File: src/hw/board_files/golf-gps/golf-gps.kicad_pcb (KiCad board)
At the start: 4 copper layers, 71.6 x 92.1 mm, 63 parts, among them J1 USB_C_Receptacle_PowerOnly_6P, J3 Micro_SD_Card, SW1 SW_SPDT, SW2 RESET, SW3 BOOT, SW4 BTN_1, SW5 BTN_2, SW6 BTN_3, U1 MCP73831-2-OT, U2 TPS63031DSKR, U3 STM32L432KCU6, U4 NEO-M9N, Y1 32.768kHz

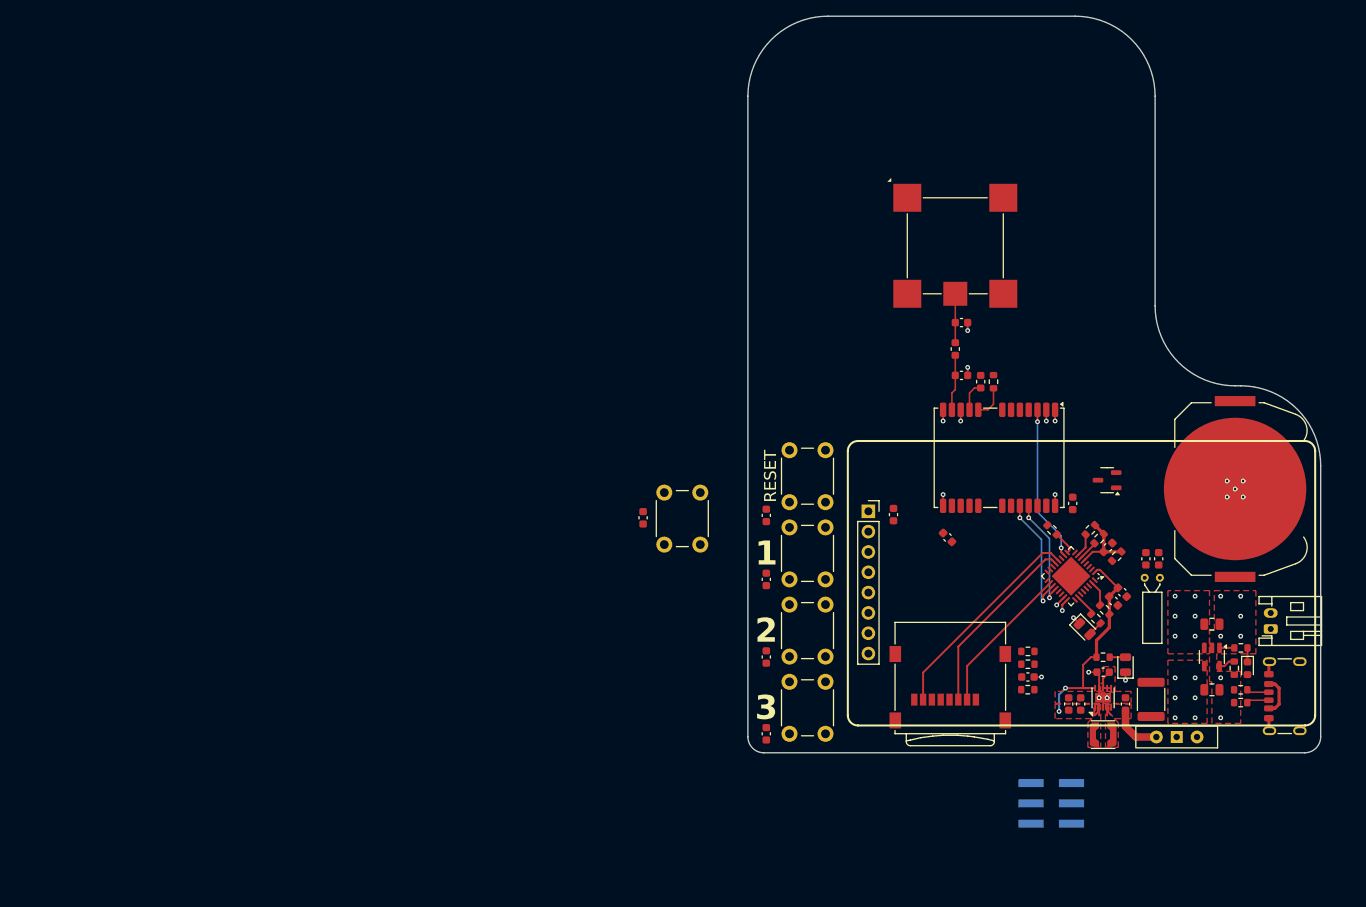
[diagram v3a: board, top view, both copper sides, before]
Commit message: Finished new sch. Updated pinout. Started new PCB.
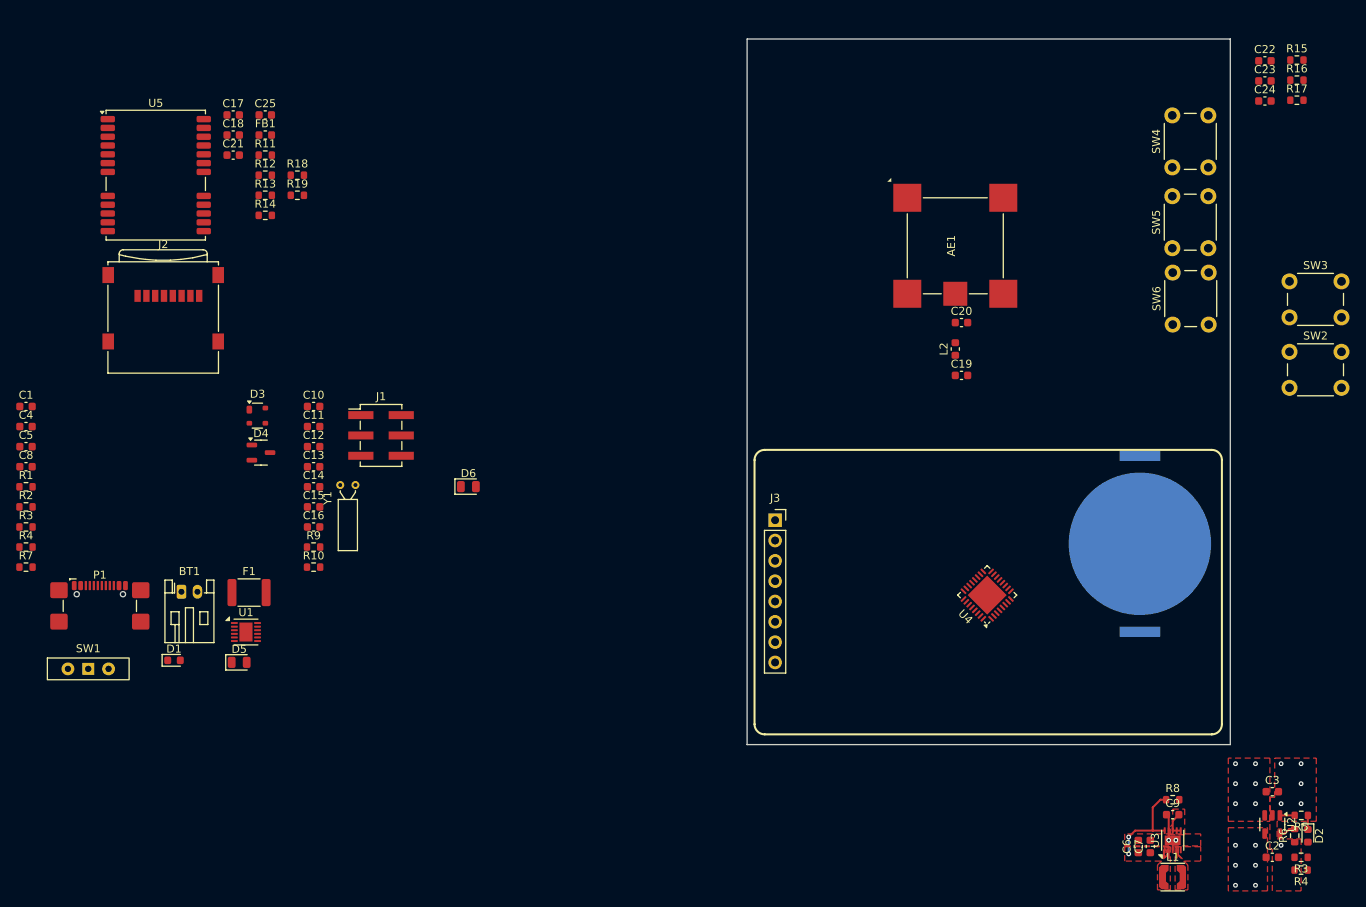
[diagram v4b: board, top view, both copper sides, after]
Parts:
- removed the C19 at (112.3, 134.0)
- removed the C20 at (112.3, 143.7)
- removed the C7 at (156.8, 135.6)
- removed the C9 at (155.0, 130.0)
- removed the J3 at (135.3, 147.5)
- removed the R6 at (156.1, 131.1)
- removed the R8 at (145.0, 147.8)
- removed the U3 at (150.4, 133.6)
- added C1: 100n, Capacitor_SMD:C_0603_1608Metric, F.Cu at (19.8, 112.4)
- added C16: TBD, Capacitor_SMD:C_0603_1608Metric, F.Cu at (55.7, 127.4)
- added C17: 100n, Capacitor_SMD:C_0603_1608Metric, F.Cu at (45.7, 75.9)
- added C23: 100n, Capacitor_SMD:C_0603_1608Metric, F.Cu at (174.6, 71.7)
- added C24: 100n, Capacitor_SMD:C_0603_1608Metric, F.Cu at (174.6, 74.2)
- added C25: 100n, Capacitor_SMD:C_0603_1608Metric, F.Cu at (49.7, 75.9)
- added C4: 47p, Capacitor_SMD:C_0603_1608Metric, F.Cu at (19.8, 114.9)
- added D5: LED_PWR, LED_SMD:LED_0805_2012Metric, F.Cu at (46.4, 144.4)
- added D6: LED_STATUS, LED_SMD:LED_0805_2012Metric, F.Cu at (75.1, 122.4)
- added P1: USB_C_Plug_USB2.0, Connector_USB:USB_C_Receptacle_GCT_USB4110, F.Cu at (29.0, 138.5)
- added R1: 27R, Resistor_SMD:R_0603_1608Metric, F.Cu at (19.8, 122.4)
- added R16: 10k, Resistor_SMD:R_0603_1608Metric, F.Cu at (178.6, 71.6)
- added R17: 10k, Resistor_SMD:R_0603_1608Metric, F.Cu at (178.6, 74.1)
- added R18: 10k, Resistor_SMD:R_0603_1608Metric, F.Cu at (53.7, 83.5)
- added R19: 10k, Resistor_SMD:R_0603_1608Metric, F.Cu at (53.7, 86.0)
- added R2: 27R, Resistor_SMD:R_0603_1608Metric, F.Cu at (19.8, 124.9)
- added R3: 1k, Resistor_SMD:R_0603_1608Metric, F.Cu at (19.8, 127.4)
- added R4: 10k, Resistor_SMD:R_0603_1608Metric, F.Cu at (19.8, 130.0)
- added U1: FT234XD-R, Package_DFN_QFN:DFN-12-1EP_3x3mm_P0.45mm_EP1.65x2.38mm, F.Cu at (47.3, 140.6)
- added U5: NEO-M9N, RF_GPS:ublox_NEO, F.Cu at (36.0, 83.5)
- BT1: value CR2032 -> LiPo; footprint Battery:BatteryHolder_Keystone_3034_1x20mm -> Connector_JST:JST_PH_S2B-PH-K_1x02_P2.00mm_Horizontal
- BT2: value LiPo -> CR2032; footprint Connector_JST:JST_PH_S2B-PH-K_1x02_P2.00mm_Horizontal -> Battery:BatteryHolder_Keystone_3034_1x20mm; moved to B.Cu
- C10: value 100n -> 2u2
- C12, C13: value TBD -> 100n
- C15: value 100n -> TBD
- C2: renamed from C1; footprint Capacitor_SMD:C_0805_2012Metric -> Capacitor_SMD:C_0603_1608Metric
- C3: renamed from C2; footprint Capacitor_SMD:C_0805_2012Metric -> Capacitor_SMD:C_0603_1608Metric
- C5: value 10u -> 47p
- C8: value 100n -> 10u
- D1: value BAT54C -> TX_LED; footprint Package_TO_SOT_SMD:SOT-23-3 -> LED_SMD:LED_0603_1608Metric
- D3: value LED_PWR -> PRTR5V0U2X; footprint LED_SMD:LED_0805_2012Metric -> Package_TO_SOT_SMD:SOT-143
- D4: value LED_STATUS -> BAT54C; footprint LED_SMD:LED_0805_2012Metric -> Package_TO_SOT_SMD:SOT-23-3
- J1: value USB_C_Receptacle_PowerOnly_6P -> ~; footprint Connector_USB:USB_C_Receptacle_GCT_USB4125-xx-x-0190_6P_TopMnt_Horizontal -> Connector_PinHeader_2.54mm:PinHeader_2x03_P2.54mm_Vertical_SMD
- J2: value ~ -> Micro_SD_Card; footprint Connector_PinHeader_2.54mm:PinHeader_2x03_P2.54mm_Vertical_SMD -> Connector_Card:microSD_HC_Wuerth_693072010801; moved to F.Cu
- R10: value 10k -> 330R
- R7: value 330R -> 5k1
- U4: value NEO-M9N -> STM32L432KCU6; footprint RF_GPS:ublox_NEO -> Package_DFN_QFN:QFN-32-1EP_5x5mm_P0.5mm_EP3.45x3.45mm
- moved C5 141.2 mm to (19.8, 117.4), turned to 0 degrees
- moved C8 137.0 mm to (19.8, 119.9), turned to 0 degrees
- moved SW1 136.3 mm to (27.5, 145.2), turned to 0 degrees
- moved R7 133.9 mm to (19.8, 132.5), turned to 0 degrees
- moved BT1 132.3 mm to (39.2, 135.5), turned to 0 degrees
- moved J2 127.1 mm to (36.9, 100.1), turned to 0 degrees
- moved D1 118.8 mm to (38.3, 144.1), turned to 0 degrees
- moved J1 118.6 mm to (64.1, 116.0), turned to 0 degrees
- moved R12 118.2 mm to (49.7, 83.5), turned to 0 degrees
- moved F1 113.5 mm to (47.6, 135.6), turned to 0 degrees
- moved D3 112.9 mm to (48.7, 113.5), turned to 0 degrees
- moved R13 112.7 mm to (49.7, 86.0), turned to 0 degrees
- moved R14 110.4 mm to (49.7, 88.5), turned to 0 degrees
- moved C12 106.6 mm to (55.7, 117.4), turned to 0 degrees
- moved D4 105.3 mm to (49.1, 118.2), turned to 0 degrees
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- renumbered C16 to C19, C17 to C20, C3 to C6, C4 to C7, C6 to C9, J4 to J3, R1 to R5, R2 to R6, R5 to R8, U1 to U2, U2 to U3
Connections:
- BT1 pad 1: Net-(BT1-+) -> VBAT
- BT2 pad 1: VBAT -> Net-(BT2-+)
- C11 pad 1: GND -> +3V3
- C11 pad 2: /Microcontroller/NRST -> GND
- C12 pad 1: Net-(U3-PC14) -> +3V3
- C13 pad 1: Net-(U3-PC15) -> +3V3
- C14 pad 1: +3V3 -> GND
- C14 pad 2: GND -> /Microcontroller/NRST
- C15 pad 1: +3V3 -> /Microcontroller/OSC32_IN
- C18 pad 1: GND -> +3V3
- C18 pad 2: /Microcontroller/BOOT -> GND
- C19 pad 1: Net-(U4-RF_IN) -> Net-(U5-RF_IN)
- C2 pad 1: /Power/V_USB -> V_USB
- C21 pad 1: GND -> /Microcontroller/BOOT0
- C21 pad 2: /Microcontroller/BTN_3 -> +3V3
- C22 pad 1: +3V3 -> GND
- C22 pad 2: GND -> /Microcontroller/BTN_1
- C5 pad 1: Net-(SW1-A) -> /Power/USB_D-
- C8 pad 1: +3V3 -> Net-(SW1-A)
- D1 pad 1: +3V3 -> Net-(D1-K)
- D1 pad 2: Net-(BT1-+) -> Net-(D1-A)
- D2 pad 2: /Power/V_USB -> V_USB
- D3 pad 2: Net-(D3-A) -> /Power/USB_D+
- D4 pad 1: GND -> +3V3
- D4 pad 2: Net-(D4-A) -> Net-(BT2-+)
- FB1 pad 1: Net-(U4-VCC_RF) -> Net-(U5-VCC_RF)
- J2 pad 1: +3V3 -> unconnected-(J2-DAT2-Pad1)
- J2 pad 2: /Microcontroller/SWDIO -> /Microcontroller/SD_CS
- J2 pad 3: GND -> /Microcontroller/SPI3_MOSI
- J2 pad 4: /Microcontroller/SWCLK -> +3V3
- J2 pad 5: GND -> /Microcontroller/SPI3_SCK
- J2 pad 6: /Microcontroller/NRST -> GND
- J3 pad 1: +3V3 -> Net-(J3-BL)
- J3 pad 4: +3V3 -> Net-(J3-BL)
- J3 pad 5: /Microcontroller/SPI_MOSI -> /Microcontroller/SPI3_MOSI
- J3 pad 6: /Microcontroller/SPI_SCK -> /Microcontroller/SPI3_SCK
- L2 pad 1: Net-(U4-RF_IN) -> Net-(U5-RF_IN)
- R10 pad 1: +3V3 -> /Microcontroller/LED_STATUS
- R10 pad 2: /Microcontroller/SPI_MISO -> Net-(D6-A)
- R11 pad 1: Net-(U4-~{RESET}) -> +3V3
- R11 pad 2: +3V3 -> /Microcontroller/SD_CS
- R12 pad 2: /Microcontroller/BOOT -> /Microcontroller/SPI3_MOSI
- R13 pad 1: /Microcontroller/BTN_1 -> +3V3
- R13 pad 2: +3V3 -> /Microcontroller/SPI3_MISO
- R14 pad 1: /Microcontroller/BTN_2 -> Net-(U5-~{RESET})
- R15 pad 1: /Microcontroller/BTN_3 -> /Microcontroller/BTN_1
- R7 pad 1: Net-(U3-PB3) -> GND
- R7 pad 2: Net-(D4-A) -> Net-(P1-CC)
- R8 pad 2: Net-(D3-A) -> Net-(D5-A)
- R9 pad 2: /Microcontroller/SPI_MOSI -> /Microcontroller/NRST
- SW3 pad 1: /Microcontroller/BOOT -> +3V3
- SW3 pad 2: GND -> /Microcontroller/BOOT0
- U2 pad 4: /Power/V_USB -> V_USB
- U4 pad 1: GND -> +3V3
- U4 pad 10: GND -> /Microcontroller/GPS_PPS
- U4 pad 11: Net-(U4-RF_IN) -> unconnected-(U4-PA5-Pad11)
- U4 pad 12: GND -> /Microcontroller/BTN_3
- U4 pad 13: GND -> /Microcontroller/BTN_2
- U4 pad 14: unconnected-(U4-LNA_EN-Pad14) -> /Microcontroller/BTN_1
- U4 pad 15: unconnected-(U4-RESERVED-Pad15) -> /Microcontroller/LED_STATUS
- U4 pad 16: unconnected-(U4-RESERVED-Pad16) -> GND
- U4 pad 17: unconnected-(U4-RESERVED-Pad17) -> +3V3
- U4 pad 19: unconnected-(U4-SCL/SPI_CLK-Pad19) -> /Microcontroller/GPS_RX
- U4 pad 2: GND -> /Microcontroller/OSC32_IN
- U4 pad 20: /Microcontroller/GPS_RX -> /Microcontroller/GPS_TX
- U4 pad 21: /Microcontroller/GPS_TX -> /Microcontroller/LCD_CS
- U4 pad 22: V_BCKP -> /Microcontroller/LCD_DC
- U4 pad 23: +3V3 -> /Microcontroller/SWDIO
- U4 pad 24: GND -> /Microcontroller/SWCLK
- U4 pad 3: /Microcontroller/GPS_PPS -> /Microcontroller/OSC32_OUT
- U4 pad 4: unconnected-(U4-EXTINT-Pad4) -> /Microcontroller/NRST
- U4 pad 5: unconnected-(U4-USB_DM-Pad5) -> +3V3
- U4 pad 8: Net-(U4-~{RESET}) -> /Microcontroller/USART2_TX
- U4 pad 9: Net-(U4-VCC_RF) -> /Microcontroller/USART2_RX
- Y1 pad 1: Net-(U3-PC15) -> /Microcontroller/OSC32_OUT
- Y1 pad 2: Net-(U3-PC14) -> /Microcontroller/OSC32_IN
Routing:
- net /Microcontroller/SPI_MISO: track 26.9 -> 0.00 mm
- net /Microcontroller/SPI_MOSI: track 23.6 -> 0.00 mm
- net +3V3: track 36.5 -> 13.0 mm
- net /Microcontroller/GPS_PPS: track 19.6 -> 0.00 mm, vias 2 -> 0
- net /Microcontroller/SD_CS: track 18.9 -> 0.00 mm
- net GND: track 22.6 -> 4.73 mm, vias 26 -> 8
- net /Microcontroller/GPS_RX: track 15.5 -> 0.00 mm, vias 2 -> 0
- net /Microcontroller/GPS_TX: track 14.1 -> 0.00 mm, vias 2 -> 0
- net Net-(U4-RF_IN): track 6.99 -> 0.00 mm
- net Net-(SW1-A): track 6.30 -> 0.00 mm
- net Net-(AE1-A): track 6.11 -> 0.00 mm
- net /Power/V_USB: track 4.99 -> 0.00 mm, vias 6 -> 0
- net Net-(U4-~{RESET}): track 4.18 -> 0.00 mm
- net Net-(U4-VCC_RF): track 3.76 -> 0.00 mm
- net /Microcontroller/BOOT: track 3.19 -> 0.00 mm
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- added copper zone on In2.Cu, net +3V3
- added copper zone on F.Cu, net V_USB
- removed copper zone on F.Cu, net /Power/V_USB
- removed copper zone on In2.Cu, net GND
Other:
- board size 71.6 x 92.1 mm -> 60.4 x 88.2 mm
- board text removed: "1"
- board text removed: "2"
- board text removed: "3"
- board text removed: "RESET"

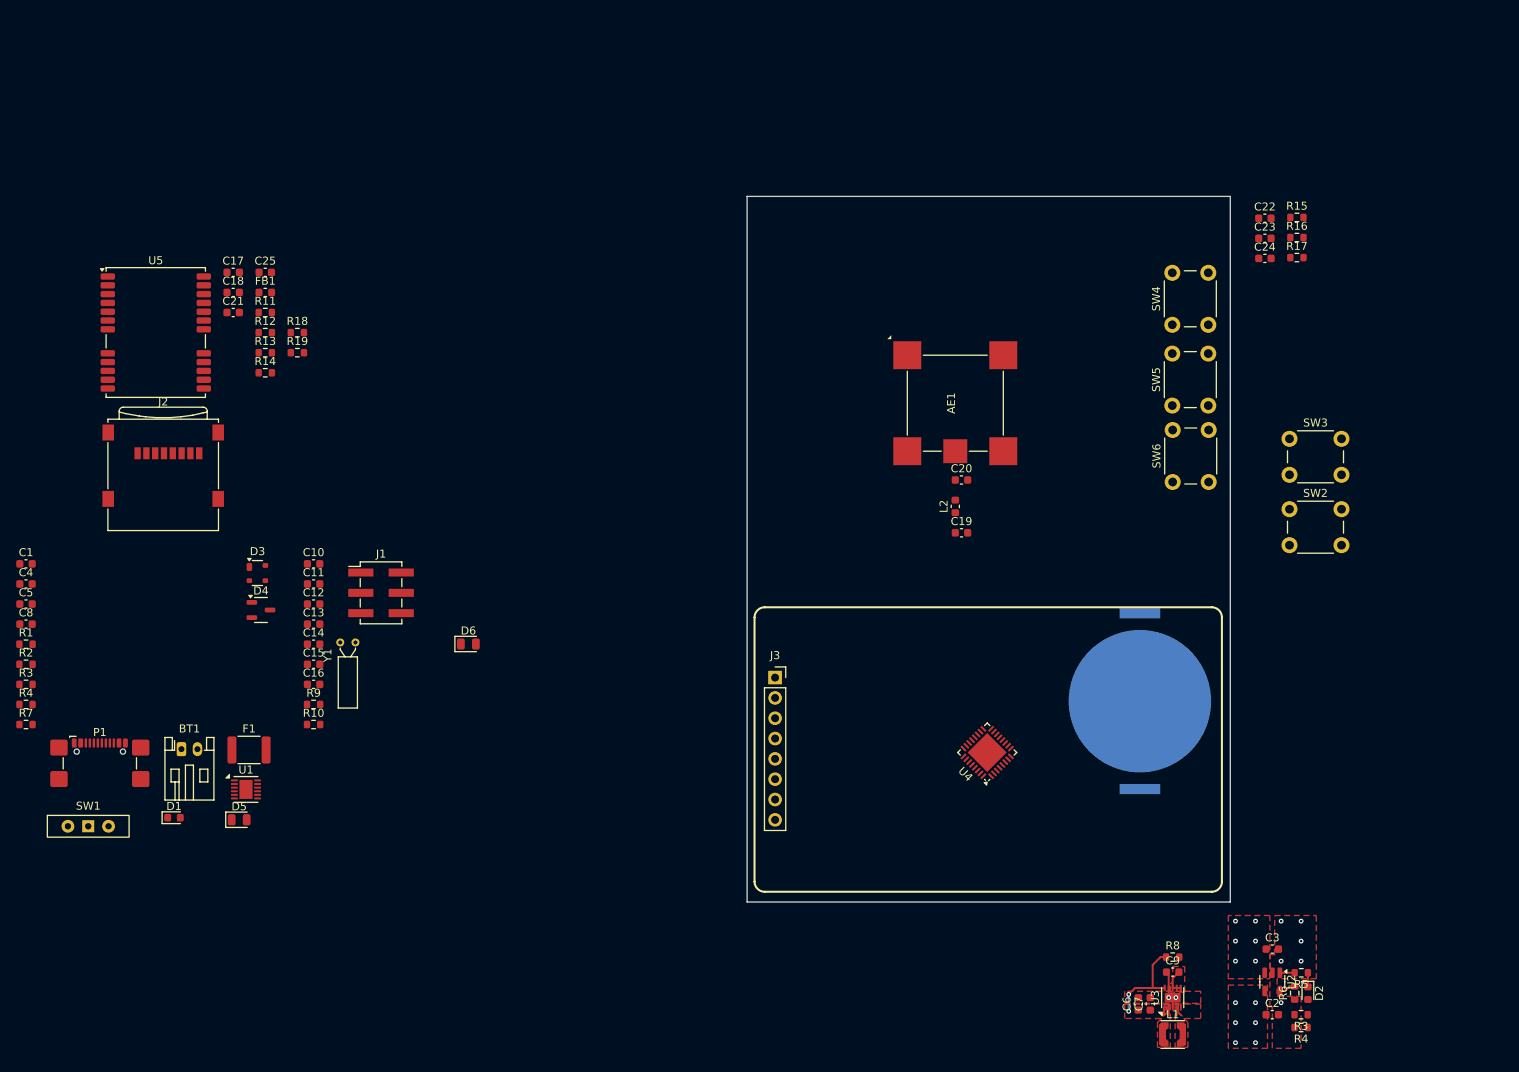
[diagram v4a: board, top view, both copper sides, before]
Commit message: Removed USB to UART bridge, added VDDA decoupling, adjusted MCU pinout and updated spreadsheet
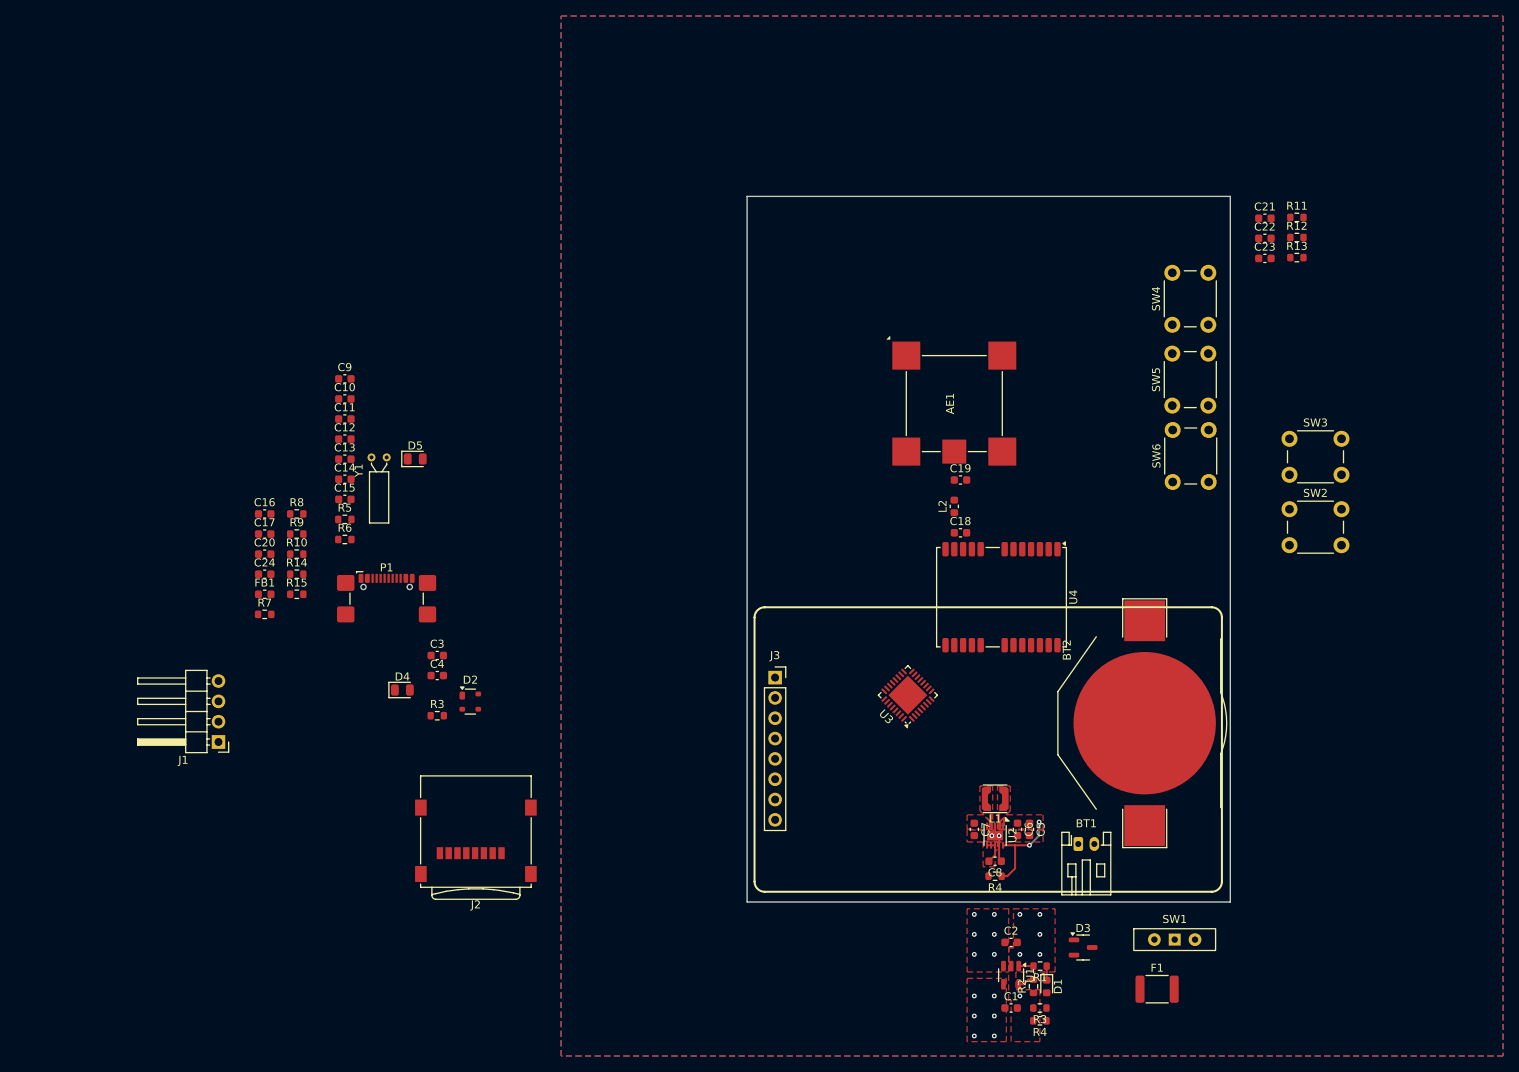
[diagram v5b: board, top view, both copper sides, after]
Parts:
- removed the C1 at (19.8, 112.4)
- removed the C18 at (45.7, 78.5)
- removed the C21 at (45.7, 81.0)
- removed C25: 100n, Capacitor_SMD:C_0603_1608Metric
- removed the C5 at (19.8, 117.4)
- removed the C8 at (19.8, 119.9)
- removed the D1 at (38.3, 144.1)
- removed D6: LED_STATUS, LED_SMD:LED_0805_2012Metric
- removed the R1 at (19.8, 122.4)
- removed the R11 at (49.7, 81.0)
- removed the R12 at (49.7, 83.5)
- removed the R13 at (49.7, 86.0)
- removed R18, R19: 10k, Resistor_SMD:R_0603_1608Metric
- removed the R2 at (19.8, 124.9)
- removed the R4 at (19.8, 130.0)
- removed the U1 at (47.3, 140.6)
- removed U5: NEO-M9N, RF_GPS:ublox_NEO
- added C20: 100n, Capacitor_SMD:C_0603_1608Metric, F.Cu at (49.6, 111.2)
- added C24: 100n, Capacitor_SMD:C_0603_1608Metric, F.Cu at (49.6, 113.7)
- added C3: 47p, Capacitor_SMD:C_0603_1608Metric, F.Cu at (71.2, 123.8)
- added C7: 10u, Capacitor_SMD:C_0603_1608Metric, F.Cu at (138.3, 145.6)
- added C9: 2u2, Capacitor_SMD:C_0603_1608Metric, F.Cu at (59.6, 89.3)
- added D2: PRTR5V0U2X, Package_TO_SOT_SMD:SOT-143, F.Cu at (75.3, 129.6)
- added R15: 10k, Resistor_SMD:R_0603_1608Metric, F.Cu at (53.6, 116.2)
- added R5: 10k, Resistor_SMD:R_0603_1608Metric, F.Cu at (59.6, 106.8)
- added R6: 330R, Resistor_SMD:R_0603_1608Metric, F.Cu at (59.6, 109.3)
- added R8: 10k, Resistor_SMD:R_0603_1608Metric, F.Cu at (53.6, 106.1)
- added U4: NEO-M9N, RF_GPS:ublox_NEO, F.Cu at (141.7, 116.5)
- BT2: footprint Battery:BatteryHolder_Keystone_3034_1x20mm -> Battery:BatteryHolder_Keystone_3002_1x2032; moved to F.Cu
- C10: value 2u2 -> 100n
- C14: value 100n -> TBD
- C16: value TBD -> 100n
- D3: value PRTR5V0U2X -> BAT54C; footprint Package_TO_SOT_SMD:SOT-143 -> Package_TO_SOT_SMD:SOT-23-3
- D4: value BAT54C -> LED_PWR; footprint Package_TO_SOT_SMD:SOT-23-3 -> LED_SMD:LED_0805_2012Metric
- D5: value LED_PWR -> LED_STATUS
- J1: value ~ -> Conn_01x04_Pin; footprint Connector_PinHeader_2.54mm:PinHeader_2x03_P2.54mm_Vertical_SMD -> Connector_PinHeader_2.54mm:PinHeader_1x04_P2.54mm_Horizontal
- R10: value 330R -> 10k
- R3: value 1k -> 5k1
- R7: value 5k1 -> 10k
- moved SW1 136.5 mm to (163.3, 159.3)
- moved F1 117.4 mm to (161.2, 165.6)
- moved D3 113.3 mm to (151.9, 160.3)
- moved BT1 112.7 mm to (151.3, 147.4)
- moved J2 61.0 mm to (76.0, 147.0), turned to 180 degrees
- moved C4 52.7 mm to (71.2, 126.3)
- moved R3 51.6 mm to (71.2, 131.4)
- moved D5 50.2 mm to (68.4, 99.3)
- moved P1 41.3 mm to (64.8, 117.9)
- moved FB1 37.7 mm to (49.6, 116.2)
- moved L1 36.9 mm to (140.9, 141.8), turned to 180 degrees
- moved C17 32.9 mm to (49.6, 108.7)
- moved R7 32.9 mm to (49.6, 118.7)
- moved C1 32.7 mm to (142.9, 167.9)
- moved C2 32.7 mm to (142.9, 159.7)
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- renumbered C2 to C1, C19 to C18, C20 to C19, C3 to C2, C22 to C21, C23 to C22, C24 to C23, C6 to C5, C7 to C6, C9 to C8, D2 to D1, R5 to R1, R15 to R11, R16 to R12, R17 to R13, R6 to R2, R8 to R4, U2 to U1, U3 to U2, U4 to U3
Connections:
- C13 pad 1: +3V3 -> GND
- C13 pad 2: GND -> /Microcontroller/NRST
- C14 pad 1: GND -> /Microcontroller/OSC32_IN
- C14 pad 2: /Microcontroller/NRST -> GND
- C15 pad 1: /Microcontroller/OSC32_IN -> /Microcontroller/OSC32_OUT
- C16 pad 1: /Microcontroller/OSC32_OUT -> +3V3
- C4 pad 1: /Power/USB_D+ -> /Microcontroller/USB_D-
- D3 pad 1: GND -> +3V3
- D3 pad 2: /Power/USB_D+ -> Net-(BT2-+)
- D3 pad 3: /Power/USB_D- -> V_BCKP
- D4 pad 1: +3V3 -> GND
- D4 pad 2: Net-(BT2-+) -> Net-(D4-A)
- J1 pad 2: /Microcontroller/SWDIO -> /Microcontroller/SWCLK
- J1 pad 3: GND -> /Microcontroller/SWDIO
- J1 pad 4: /Microcontroller/SWCLK -> GND
- P1 pad A6: /Power/USB_D+ -> /Microcontroller/USB_D+
- P1 pad A7: /Power/USB_D- -> /Microcontroller/USB_D-
- R10 pad 1: /Microcontroller/LED_STATUS -> Net-(U4-~{RESET})
- R10 pad 2: Net-(D6-A) -> +3V3
- R14 pad 1: Net-(U5-~{RESET}) -> /Microcontroller/BOOT0
- R14 pad 2: +3V3 -> GND
- R3 pad 1: Net-(D1-A) -> GND
- R3 pad 2: +3V3 -> Net-(P1-CC)
- R4 pad 2: Net-(D5-A) -> Net-(D4-A)
- R7 pad 1: GND -> +3V3
- R7 pad 2: Net-(P1-CC) -> /Microcontroller/SD_CS
- R9 pad 2: /Microcontroller/NRST -> /Microcontroller/SPI3_MISO
- U3 pad 21: /Microcontroller/LCD_CS -> /Microcontroller/USB_D-
- U3 pad 22: /Microcontroller/LCD_DC -> /Microcontroller/USB_D+
- U3 pad 8: /Microcontroller/USART2_TX -> /Microcontroller/LCD_CS
- U3 pad 9: /Microcontroller/USART2_RX -> /Microcontroller/LCD_DC
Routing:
- net Net-(U2-L2): track 0.99 -> 1.59 mm
- net Net-(U2-L1): track 0.99 -> 1.59 mm
- added copper zone on B.Cu, net GND
